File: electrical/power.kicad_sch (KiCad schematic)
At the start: 48 parts

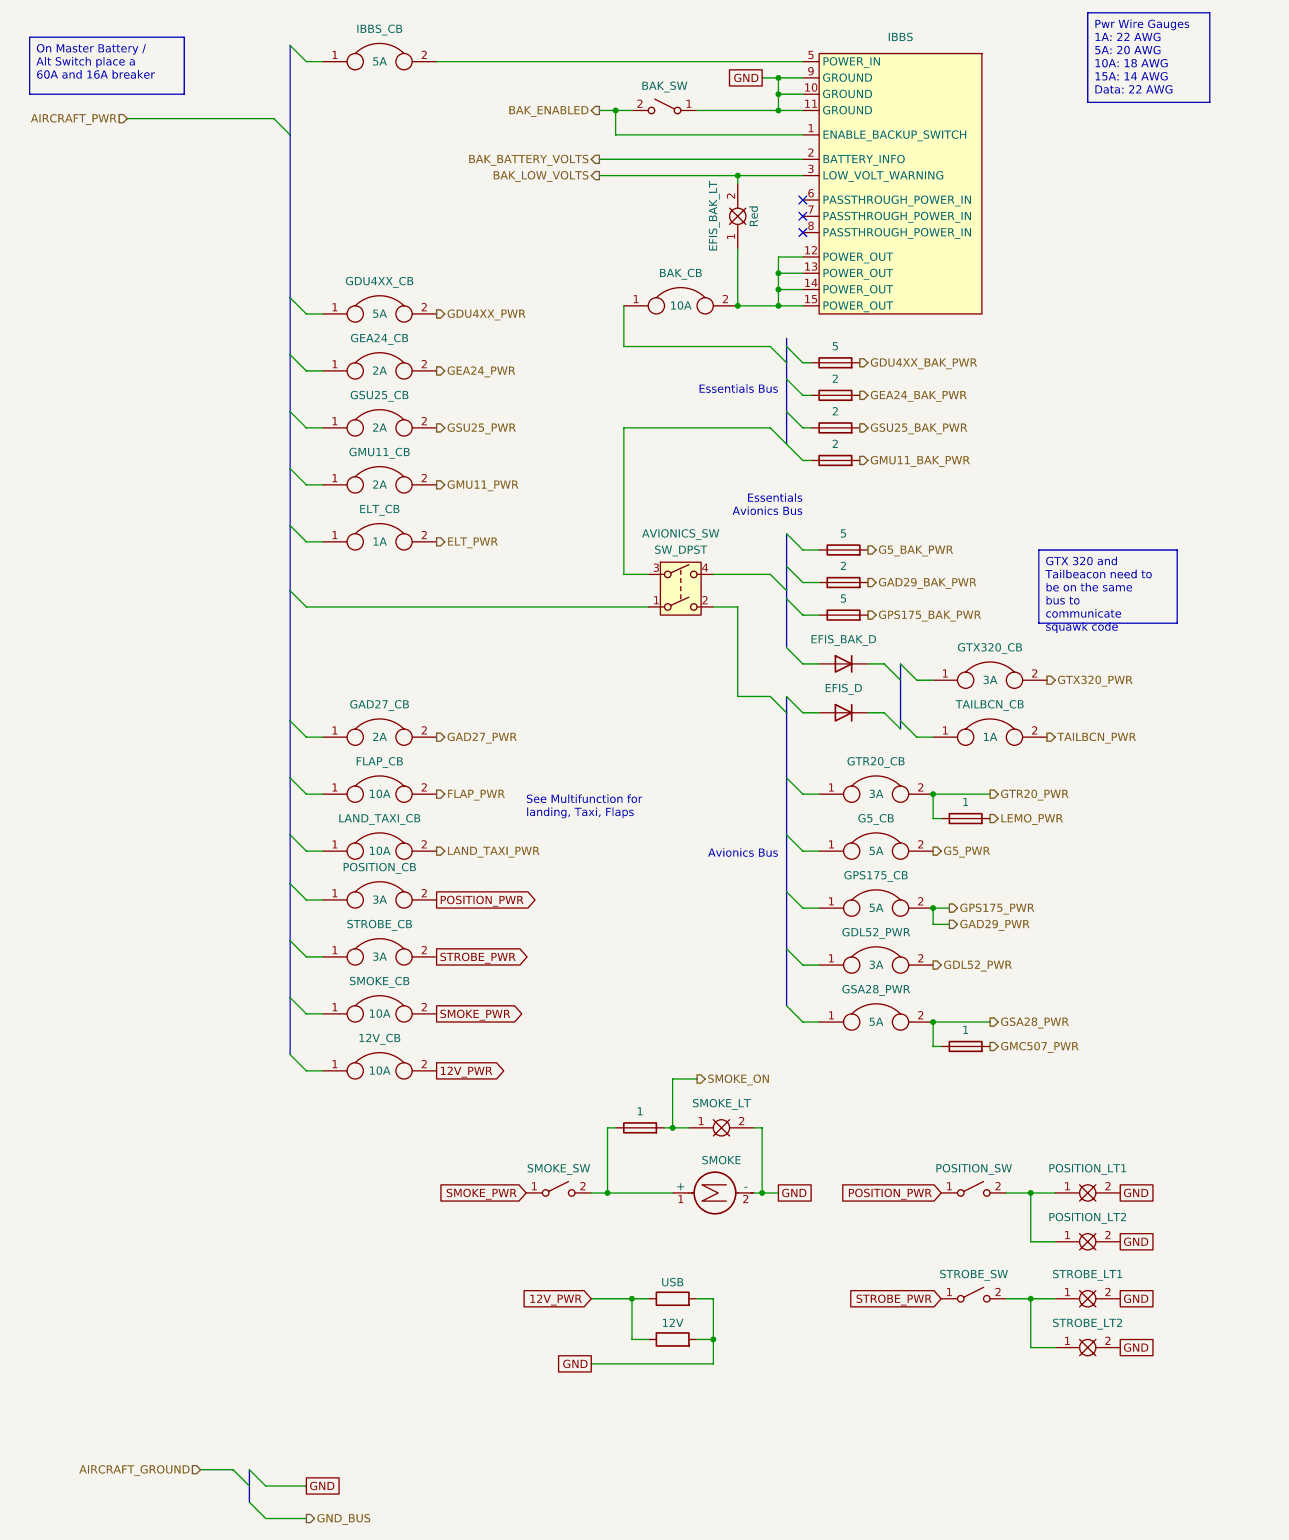
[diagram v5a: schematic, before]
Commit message: Updated electrical to not use IBBS. Also, added BT adapter and 3P3T switch.
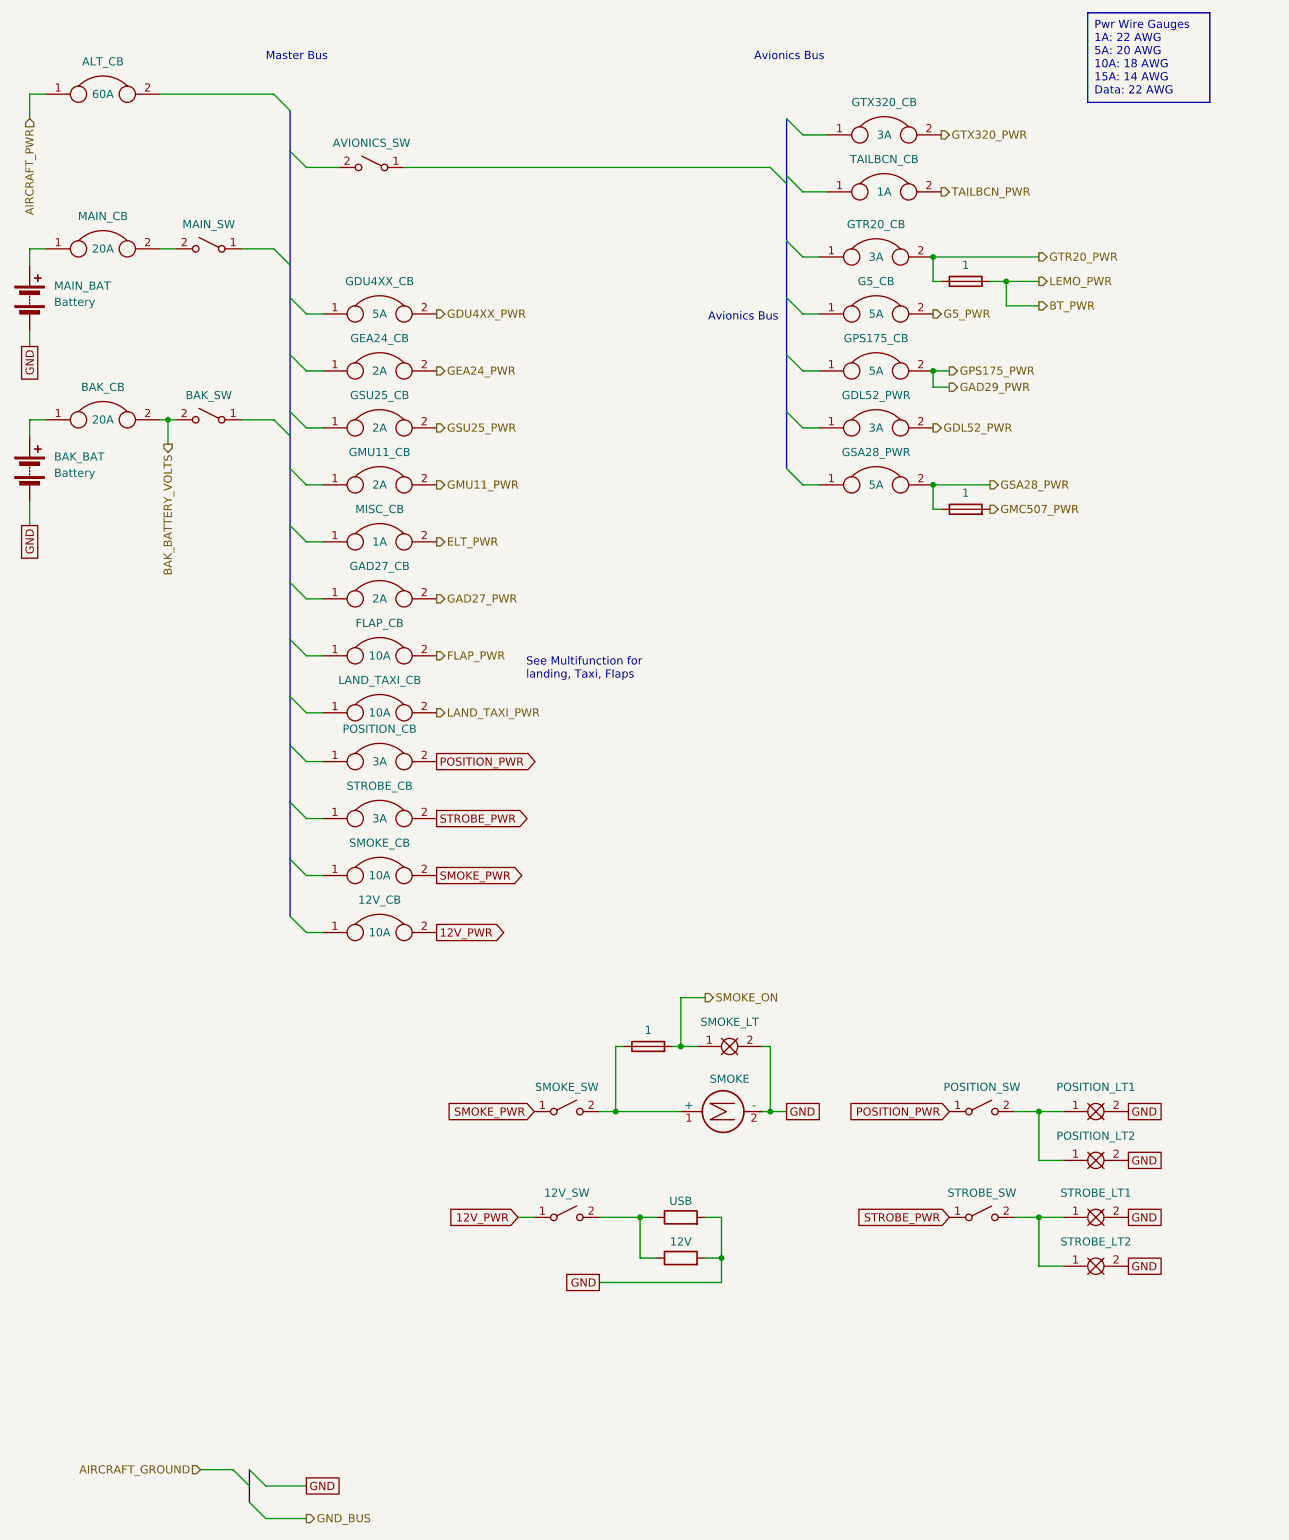
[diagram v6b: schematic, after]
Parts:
- removed AVIONICS_SW: SW_DPST, symbol Switch:SW_DPST
- removed BAK_G5_FS, BAK_GDU4XX_FS, BAK_GPS175_FS: 5, symbol Device:Fuse
- removed BAK_GAD29_FS, BAK_GEA24_FS, BAK_GMU11_FS, BAK_GSU25_FS: 2, symbol Device:Fuse
- removed EFIS_BAK_D, EFIS_D: 1N5400, Diode_THT:D_DO-201AD_P15.24mm_Horizontal, symbol Diode:1N5400
- removed EFIS_BAK_LT: Red, symbol FlyerX:Bulb
- removed IBBS: ~, symbol flyerx:TCW_IBBS-12V-3AH
- removed IBBS_CB: 5A, symbol flyerx:Circuit_Breaker
- added 12V_SW, AVIONICS_SW, MAIN_SW: ~, symbol Switch:SW_SPST
- added ALT_CB: 60A, symbol flyerx:Circuit_Breaker
- added BAK_BAT, MAIN_BAT: Battery, symbol Device:Battery
- added MAIN_CB: 20A, symbol flyerx:Circuit_Breaker
- BAK_CB: value 10A -> 20A
- renumbered ELT_CB to MISC_CB
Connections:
- net BAK_ENABLED is gone; now on net BAK_BATTERY_VOLTS: BAK_SW.2 (B)
- net 12V_PWR: now also 12V_SW.1 (A); no longer 12V.1, USB.1
- net AIRCRAFT_PWR: now also ALT_CB.1
- net BAK_BATTERY_VOLTS: now also BAK_CB.2
- net GND: now also BAK_BAT.2 (-), MAIN_BAT.2 (-); no longer BAK_SW.1 (A)
- net at BAK_CB.1: now also BAK_BAT.1 (+)
- net LEMO_PWR renamed BT_PWR
- new net: 12V.1, 12V_SW.2 (B), USB.1
- new net: MAIN_BAT.1 (+), MAIN_CB.1
- new net: MAIN_CB.2, MAIN_SW.2 (B)
- no-connect marks 3 -> 0
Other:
- note added: "Master Bus"
- note removed: "Essentials Avionics Bus"
- note removed: "Essentials Bus"
- moved on the sheet: 12V, 12V_CB, BAK_SW, FLAP_CB, G5_CB, GAD27_CB, GDL52_PWR, GPS175_CB, GSA28_PWR, GTR20_CB, GTX320_CB, LAND_TAXI_CB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

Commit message: Changed to have ELT with GPS. Also, changed Flaps to have position sensor. Added in wiring for all the sensors.
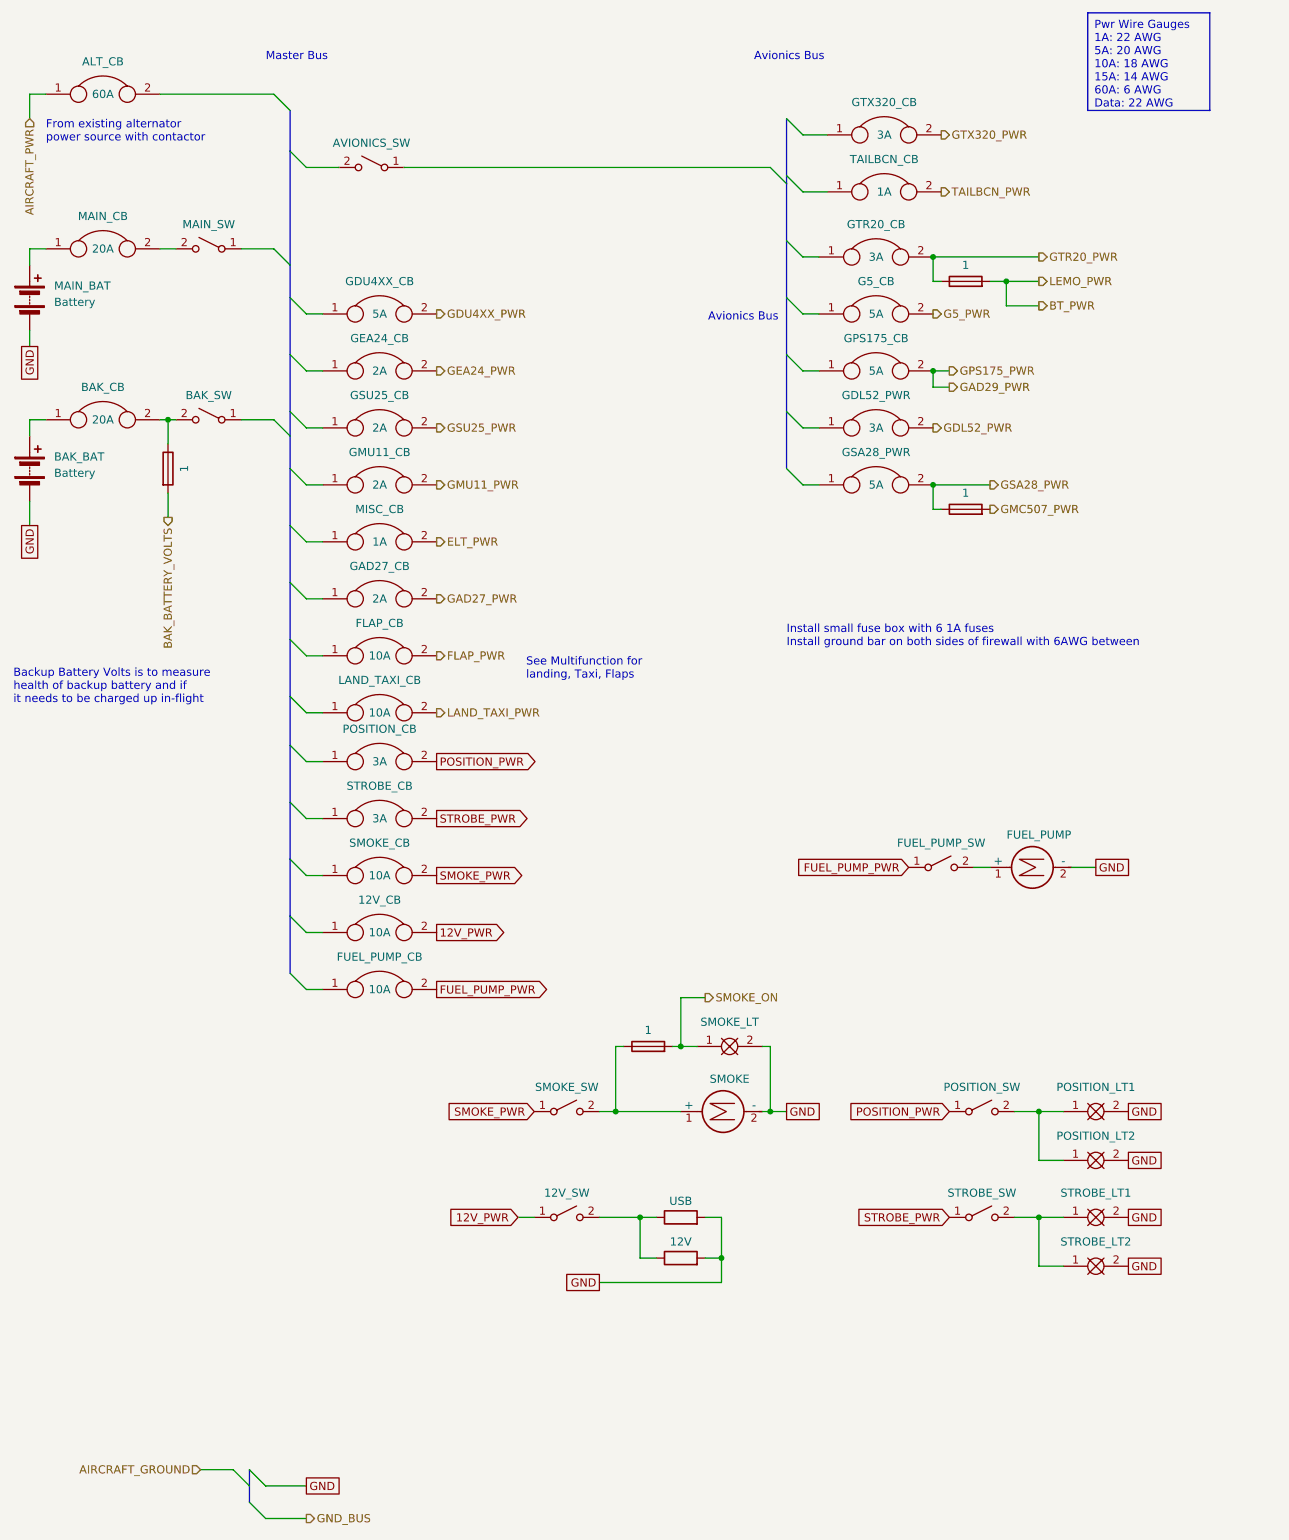
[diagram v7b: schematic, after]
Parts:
- added BAK_BAT_VOLTS_FS: 1, symbol Device:Fuse
- added FUEL_PUMP: Motor_DC, symbol Motor:Motor_DC
- added FUEL_PUMP_CB: 10A, symbol flyerx:Circuit_Breaker
- added FUEL_PUMP_SW: ~, symbol Switch:SW_SPST
- renumbered GMC507_FS1 to GMC507_FS, LEMO_FS1 to LEMO_FS
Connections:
- net BAK_BATTERY_VOLTS: now also BAK_BAT_VOLTS_FS.2; no longer BAK_CB.2, BAK_SW.2 (B)
- net GND: now also FUEL_PUMP.2 (-)
- new net: FUEL_PUMP.1 (+), FUEL_PUMP_SW.2 (B)
- new net: BAK_BAT_VOLTS_FS.1, BAK_CB.2, BAK_SW.2 (B)
- new net FUEL_PUMP_PWR: FUEL_PUMP_CB.2, FUEL_PUMP_SW.1 (A)
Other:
- note added: "Backup Battery Volts is to measure health of backup battery and if it needs to be charged up in-flight"
- note added: "From existing alternator power source with contactor"
- note added: "Install small fuse box with 6 1A fuses Install ground bar on both sides of firewall with 6AWG between"
